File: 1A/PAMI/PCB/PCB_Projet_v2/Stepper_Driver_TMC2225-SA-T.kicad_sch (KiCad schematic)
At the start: 12 parts, among them U4 TMC2225-SA-T

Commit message: update pcb
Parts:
- C19, C20, C21: footprint Capacitor_SMD:C_0603_1608Metric -> Capacitor_SMD:C_0402_1005Metric

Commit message: update PCB placement
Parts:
- R25, R26: footprint Resistor_SMD:R_0402_1005Metric -> Resistor_SMD:R_2512_6332Metric
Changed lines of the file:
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@@
 			)
 		)
-		(property "Footprint" "Resistor_SMD:R_0402_1005Metric"
+		(property "Footprint" "Resistor_SMD:R_2512_6332Metric"
 			(at 176.53 104.648 90)
 			(effects
@@
 			)
 		)
-		(property "Footprint" "Resistor_SMD:R_0402_1005Metric"
+		(property "Footprint" "Resistor_SMD:R_2512_6332Metric"
 			(at 176.53 93.218 90)
 			(effects

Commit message: update PAMI pcb
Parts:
- renumbered C19 to C201, C20 to C202, C21 to C203, D9 to D201, R21 to R201, R22 to R202, R23 to R203, R24 to R204, R25 to R205, R26 to R206, R27 to R207, U4 to U201

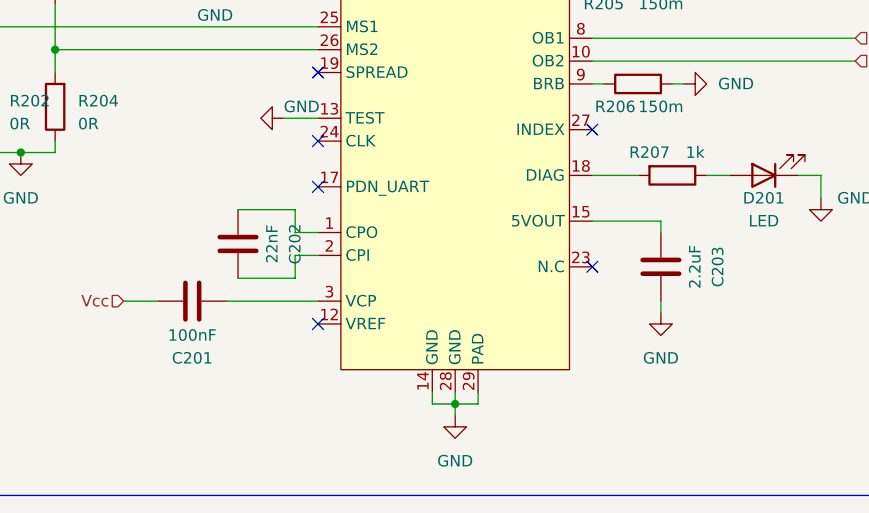
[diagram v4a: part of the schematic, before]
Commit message: add PAMI PCB Teardrops, export gerbers
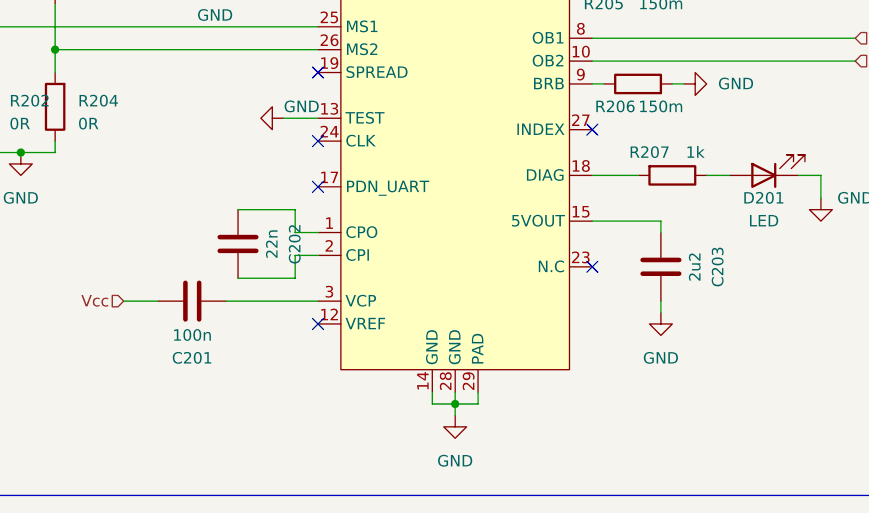
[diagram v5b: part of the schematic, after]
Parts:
- C201: value 100nF -> 100n
- C202: value 22nF -> 22n
- C203: value 2.2uF -> 2u2
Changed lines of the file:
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@@
 			)
 		)
-		(property "Value" "2.2uF"
+		(property "Value" "2u2"
 			(at 182.88 123.19 90)
 			(effects
@@
 			)
 		)
-		(property "Value" "22nF"
+		(property "Value" "22n"
 			(at 135.89 120.65 90)
 			(effects
@@
 			)
 		)
-		(property "Value" "100nF"
+		(property "Value" "100n"
 			(at 127 130.81 90)
 			(effects
